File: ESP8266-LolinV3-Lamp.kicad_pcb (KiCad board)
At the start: 2 copper layers, 46.2 x 57.9 mm, 22 parts, among them J1 Conn_01x15_Male, J2 PWR, J3 Conn_01x15_Male, J4 LED, J5 BUTTON, J6 MIC, Q1 IRLB8721PBF, Q2 IRLB8721PBF, Q3 FDN337N, Q4 FDN338P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

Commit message: Added d-diot logo
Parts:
- added G***: LOGO, logo:d-diot-logo-small, F.Cu at (158.8, 100.1)

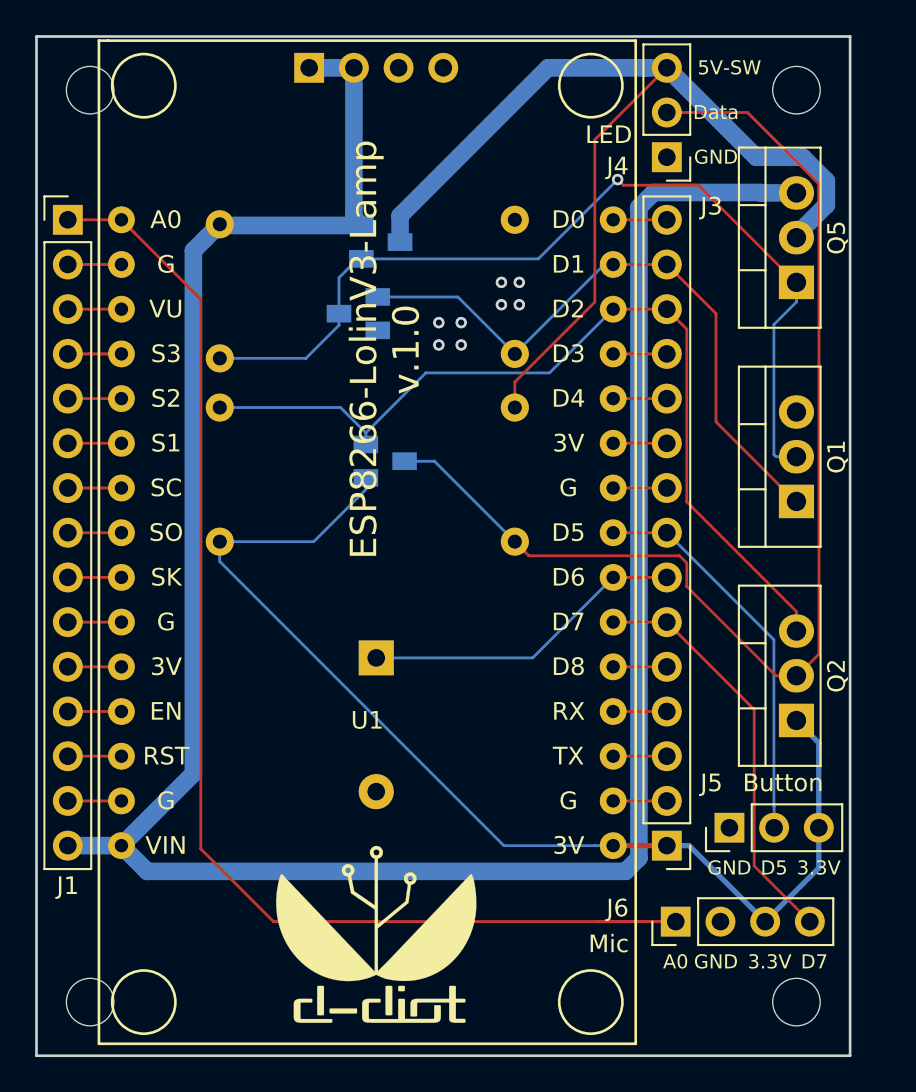
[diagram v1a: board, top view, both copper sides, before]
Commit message: added photoresistor, barrel jack, 1000uF cap, LED data pin resistor
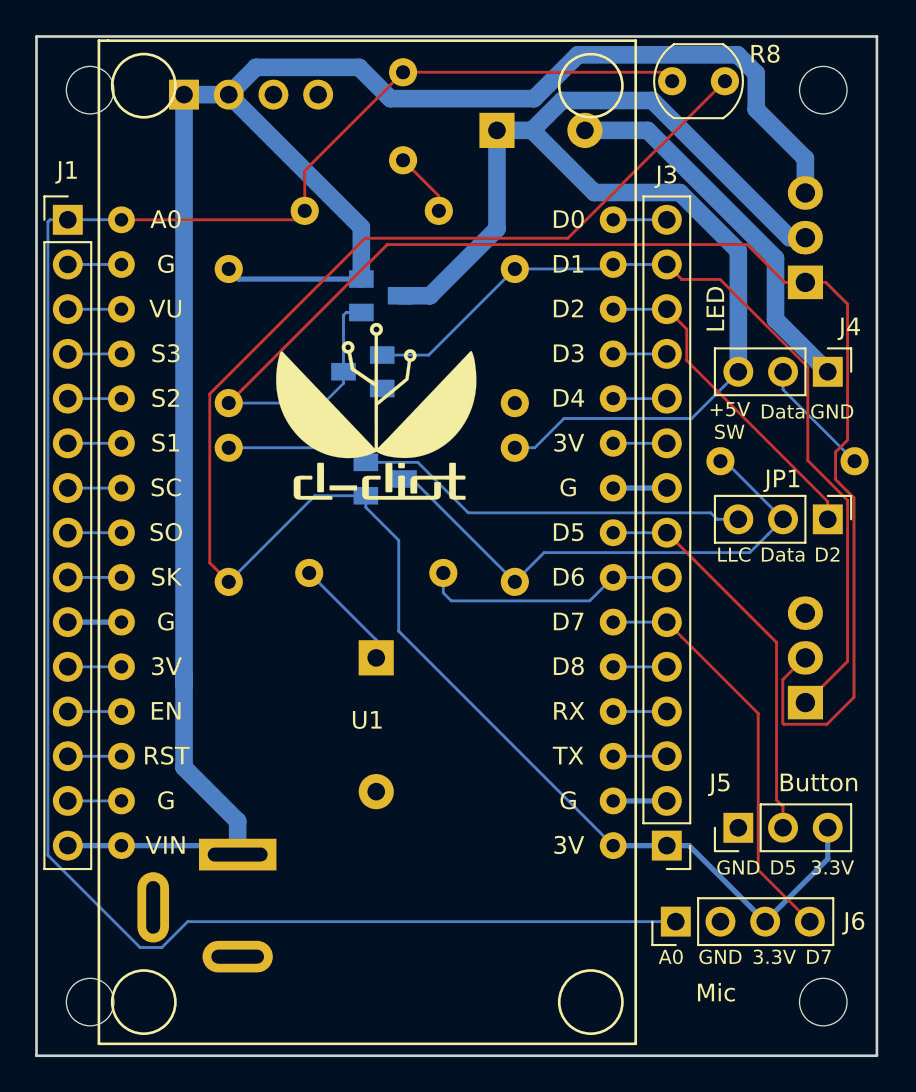
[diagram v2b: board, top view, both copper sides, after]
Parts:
- removed Q2: IRLB8721PBF, Package_TO_SOT_THT:TO-220-3_Vertical
- added C1: 1000uF, Capacitor_THT:CP_Radial_D10.0mm_P5.00mm, B.Cu at (165.6, 54.1)
- added C2: 0.1uF, Capacitor_THT:C_Disc_D6.0mm_W4.4mm_P5.00mm, B.Cu at (160.3, 50.8)
- added J7: Barrel_Jack, Connector_BarrelJack:BarrelJack_Wuerth_6941xx301002, B.Cu at (150.9, 95.2)
- added JP1: Jumper_3_Open, Connector_PinHeader_2.54mm:PinHeader_1x03_P2.54mm_Vertical, F.Cu at (184.4, 76.2)
- added R5: 470R, Resistor_THT:R_Axial_DIN0207_L6.3mm_D2.5mm_P7.62mm_Horizontal, B.Cu at (185.9, 72.9)
- added R6: 200R, Resistor_THT:R_Axial_DIN0207_L6.3mm_D2.5mm_P7.62mm_Horizontal, B.Cu at (162.6, 79.2)
- added R7: 56K, Resistor_THT:R_Axial_DIN0207_L6.3mm_D2.5mm_P7.62mm_Horizontal, B.Cu at (162.3, 58.7)
- added R8: R_PHOTO, OptoDevice:R_LDR_5.0x4.1mm_P3mm_Vertical, F.Cu at (178.6, 51.3)
- Q1, Q5: moved to B.Cu
- moved G*** 29.7 mm to (158.8, 70.4)
- moved J4 15.2 mm to (184.4, 67.8), turned to 270 degrees
- moved Q1 11.4 mm to (183.1, 86.6)
- moved J2 7.27 mm to (147.8, 52.1)
- moved R3 4.83 mm to (166.6, 62.0), turned to 270 degrees
- moved Q6 3.31 mm to (158.0, 67.8)
- moved Q4 3.05 mm to (159.0, 63.5)
- moved R4 2.59 mm to (150.4, 62.0)
- moved R2 2.34 mm to (150.4, 72.1)
- moved R1 2.29 mm to (166.6, 79.8)
- moved REF** 1.52 mm to (184.2, 51.8)
- moved REF** 1.52 mm to (184.2, 103.6)
- moved Q3 1.02 mm to (159.3, 73.9)
- moved J5 0.51 mm to (179.3, 93.7)
- moved Q5 0.51 mm to (183.1, 62.7)
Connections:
- BZ1 pad 1: D6 -> Net-(BZ1-Pad1)
- J4 pad 2: DATA -> Net-(J4-Pad2)
- Q3 pad 2: D2 -> Net-(JP1-Pad3)
- R2 pad 1: D2 -> Net-(JP1-Pad3)
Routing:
- net A0: track 75.0 -> 115.7 mm
- net DATA: track 66.9 -> 30.3 mm
- net 3.3V: track 64.0 -> 100.5 mm
- net D2: track 50.9 -> 18.8 mm
- net Net-(Q1-Pad2): track 52.7 -> 84.3 mm, vias 1 -> 0
- net Net-(JP1-Pad3): track 0.00 -> 31.0 mm
- net GND: track 3.05 -> 28.3 mm, vias 8 -> 0
- net Net-(J1-Pad15): track 137.0 -> 119.5 mm
- net D1: track 36.4 -> 49.8 mm
- net +5V: track 58.7 -> 70.1 mm
- net Net-(J4-Pad2): track 0.00 -> 6.76 mm
- net Net-(BZ1-Pad1): track 0.00 -> 6.40 mm
- net D6: track 18.4 -> 14.6 mm
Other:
- board size 46.2 x 57.9 mm -> 47.8 x 57.9 mm
- board text added: "+"
- board text added: "+5V SW"
- board text added: "D2"
- board text added: "LLC"
- board text removed: "5V-SW"

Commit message: Board version 2.0
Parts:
- removed Q1: IRLB8721PBF, Package_TO_SOT_THT:TO-220-3_Vertical
- removed Q3: FDN337N, FDN337N:SSOT-3
- removed R1, R2: 10K, Resistor_THT:R_Axial_DIN0207_L6.3mm_D2.5mm_P7.62mm_Horizontal
- added D1: 1N4007, Diode_THT:D_DO-41_SOD81_P10.16mm_Horizontal, F.Cu at (178.8, 73.4)
- added J8: FAN, Connector_PinHeader_2.54mm:PinHeader_1x02_P2.54mm_Vertical, F.Cu at (184.9, 73.9)
- added J9: PWR-2, Connector_PinHeader_2.54mm:PinHeader_1x02_P2.54mm_Vertical, F.Cu at (184.9, 81.3)
- added U2: SN74AHCT125DR, SN74AHCT125DR:SOIC127P600X175-14N, B.Cu at (159.3, 76.5)
- moved R5 20.1 mm to (167.4, 80.8), turned to 90 degrees
- moved JP1 12.0 mm to (179.3, 87.1), turned to 90 degrees
- moved R6 6.82 mm to (167.4, 84.1), turned to 270 degrees
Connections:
- J4 pad 2: Net-(J4-Pad2) -> DATA
- JP1 pad 1: D2 -> Net-(JP1-Pad1)
- R5 pad 1: Net-(J4-Pad2) -> D2
- R5 pad 2: DATA -> Net-(JP1-Pad1)
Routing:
- net 3.3V: track 100.5 -> 64.0 mm
- net Net-(Q4-Pad1): track 84.3 -> 49.3 mm
- net +5V: track 70.1 -> 103.6 mm
- net D1: track 49.8 -> 18.3 mm
- net Net-(JP1-Pad1): track 0.00 -> 24.4 mm
- net D2: track 18.8 -> 29.2 mm
- net DATA: track 30.3 -> 20.7 mm
- net Net-(J4-Pad2): track 6.76 -> 0.00 mm
- net Net-(BZ1-Pad1): track 6.40 -> 11.8 mm
- net D6: track 14.6 -> 9.77 mm
- net Net-(JP1-Pad3): track 31.0 -> 28.6 mm
- net D7: track 23.4 -> 24.0 mm
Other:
- board text added: "+5V"
- board text added: "ESP8266-LolinV3-Lamp v.2.0"
- board text added: "FAN"
- board text added: "PWR-2"
- board text removed: "+"
- board text removed: "+5V SW"
- board text removed: "ESP8266-LolinV3-Lamp v.1.0"
